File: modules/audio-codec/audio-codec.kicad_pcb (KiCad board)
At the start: 2 copper layers, 1 part, among them U1 TLV320AIC3110IRHBR

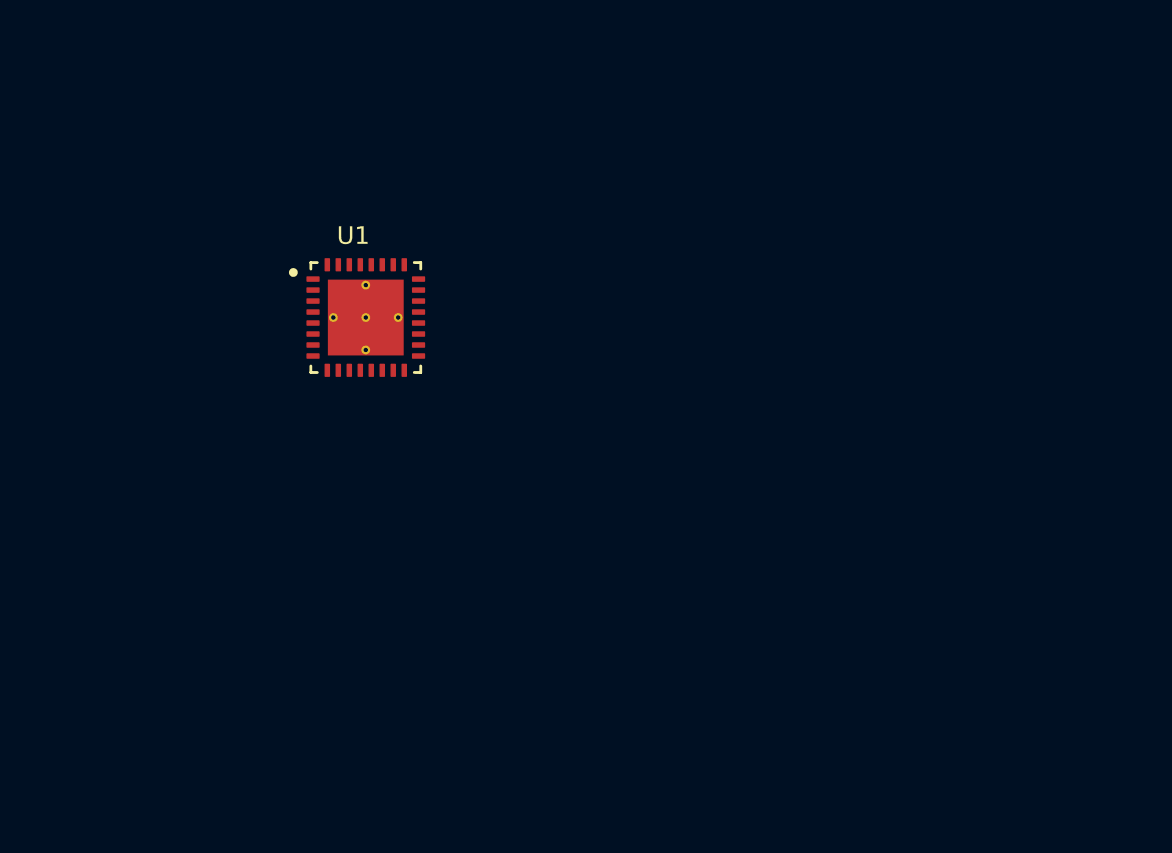
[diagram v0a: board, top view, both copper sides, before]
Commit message: update 2x11 module footprint. Work on PCB layout of audio codec module
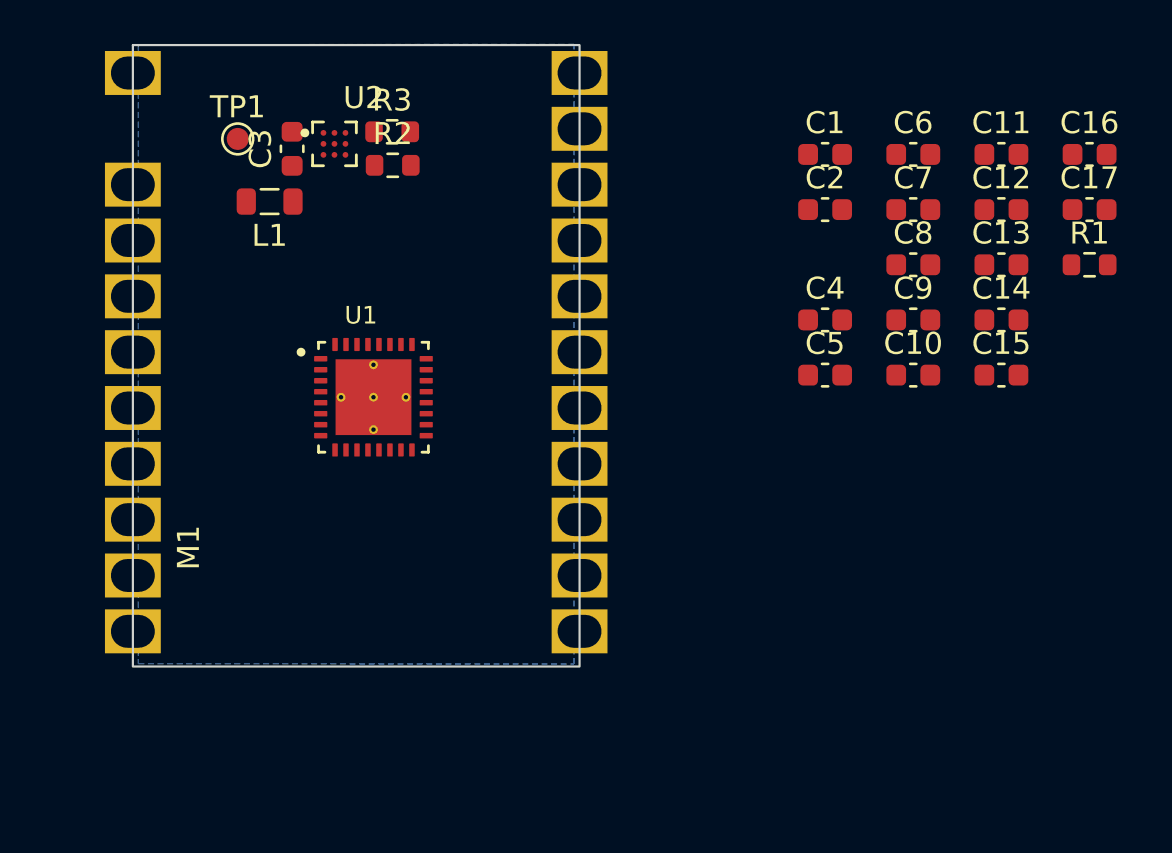
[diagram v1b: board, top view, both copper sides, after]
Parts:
- added C1: 0.1uF, Capacitor_SMD:C_0603_1608Metric, F.Cu at (106.0, 54.1)
- added C10: 0.1uF, Capacitor_SMD:C_0603_1608Metric, F.Cu at (110.0, 64.1)
- added C11: 10uF, Capacitor_SMD:C_0603_1608Metric, F.Cu at (114.0, 54.1)
- added C12: 0.1uF, Capacitor_SMD:C_0603_1608Metric, F.Cu at (114.0, 56.6)
- added C13: 0.1uF, Capacitor_SMD:C_0603_1608Metric, F.Cu at (114.0, 59.1)
- added C14: 10uF, Capacitor_SMD:C_0603_1608Metric, F.Cu at (114.0, 61.6)
- added C15: 10uF, Capacitor_SMD:C_0603_1608Metric, F.Cu at (114.0, 64.1)
- added C16: 47uF, Capacitor_SMD:C_0603_1608Metric, F.Cu at (118.0, 54.1)
- added C17: 47uF, Capacitor_SMD:C_0603_1608Metric, F.Cu at (118.0, 56.6)
- added C2: 10uF, Capacitor_SMD:C_0603_1608Metric, F.Cu at (106.0, 56.6)
- added C3: 10uF, Capacitor_SMD:C_0603_1608Metric, F.Cu at (81.8, 53.8)
- added C4: 0.1uF, Capacitor_SMD:C_0603_1608Metric, F.Cu at (106.0, 61.6)
- added C5: 22uF, Capacitor_SMD:C_0603_1608Metric, F.Cu at (106.0, 64.1)
- added C6: 0.1uF, Capacitor_SMD:C_0603_1608Metric, F.Cu at (110.0, 54.1)
- added C7: 22uF, Capacitor_SMD:C_0603_1608Metric, F.Cu at (110.0, 56.6)
- added C8: 0.1uF, Capacitor_SMD:C_0603_1608Metric, F.Cu at (110.0, 59.1)
- added C9: 10uF, Capacitor_SMD:C_0603_1608Metric, F.Cu at (110.0, 61.6)
- added L1: 2.2uH, Inductor_SMD:L_0805_2012Metric, F.Cu at (80.7, 56.2)
- added M1: ~, MegaCastle:MegaCastle2x11Wide-Module-I13.2x22.25, F.Cu at (84.7, 61.8)
- added R1: 2.2K, Resistor_SMD:R_0603_1608Metric, F.Cu at (118.0, 59.1)
- added R2: 19.6K, Resistor_SMD:R_0603_1608Metric, F.Cu at (86.3, 54.5)
- added R3: 100K, Resistor_SMD:R_0603_1608Metric, F.Cu at (86.3, 53.0)
- added TP1: 1.8V, TestPoint:TestPoint_Pad_D1.0mm, F.Cu at (79.3, 53.4)
- added U2: ADP5301ACBZ-1-R7, audio-codec:BGA9C50P3X3_187X165X66N, F.Cu at (83.7, 53.6)
- moved U1 3.64 mm to (85.5, 65.1)
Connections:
- U1 pad 1: unconnected-(U1-IOVSS-Pad1) -> GND
- U1 pad 10: unconnected-(U1-SCL-Pad10) -> SCL
- U1 pad 11: unconnected-(U1-VOL/MICDET-Pad11) -> Net-(U1-MIC1RP)
- U1 pad 12: unconnected-(U1-MICBIAS-Pad12) -> Net-(U1-MICBIAS)
- U1 pad 14: unconnected-(U1-MIC1RP-Pad14) -> Net-(U1-MIC1RP)
- U1 pad 16: unconnected-(U1-AVSS-Pad16) -> GND
- U1 pad 17: unconnected-(U1-AVDD-Pad17) -> DECOUPLE1
- U1 pad 18: unconnected-(U1-DVSS-Pad18) -> GND
- U1 pad 19: unconnected-(U1-SPLM-Pad19) -> SPEAKER_L_M
- U1 pad 2: unconnected-(U1-IOVDD-Pad2) -> DECOUPLE4
- U1 pad 20: unconnected-(U1-SPLVSS-Pad20) -> GND
- U1 pad 21: unconnected-(U1-SPLVDD-Pad21) -> DECOUPLE1
- U1 pad 22: unconnected-(U1-SPLP-Pad22) -> SPEAKER_L_P
- U1 pad 23: unconnected-(U1-SPRM-Pad23) -> SPEAKER_R_M
- U1 pad 24: unconnected-(U1-SPRVDD-Pad24) -> DECOUPLE1
- U1 pad 25: unconnected-(U1-SPRVSS-Pad25) -> GND
- U1 pad 26: unconnected-(U1-SPRP-Pad26) -> SPEAKER_R_P
- U1 pad 27: unconnected-(U1-HPL-Pad27) -> Net-(U1-HPL)
- U1 pad 28: unconnected-(U1-HPVDD-Pad28) -> DECOUPLE4
- U1 pad 29: unconnected-(U1-HPVSS-Pad29) -> GND
- U1 pad 3: unconnected-(U1-DVDD-Pad3) -> DECOUPLE5
- U1 pad 30: unconnected-(U1-HPR-Pad30) -> Net-(U1-HPR)
- U1 pad 31: unconnected-(U1-~{RESET}-Pad31) -> /RESET
- U1 pad 32: unconnected-(U1-GPIO1-Pad32) -> GPIO1
- U1 pad 33: unconnected-(U1-EP-Pad33) -> GND
- U1 pad 4: unconnected-(U1-DOUT-Pad4) -> I2S_DOUT
- U1 pad 5: unconnected-(U1-DIN-Pad5) -> I2S_DIN
- U1 pad 6: unconnected-(U1-WCLK-Pad6) -> WCLK
- U1 pad 7: unconnected-(U1-BCLK-Pad7) -> I2S_BCLK
- U1 pad 8: unconnected-(U1-MCLK-Pad8) -> I2S_MCLK
- U1 pad 9: unconnected-(U1-SDA-Pad9) -> SDA
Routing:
- added copper zone on B.Cu, net GND
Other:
- board outline added: 20.3 x 28.3 mm

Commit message: more work on audio codec PCB layout
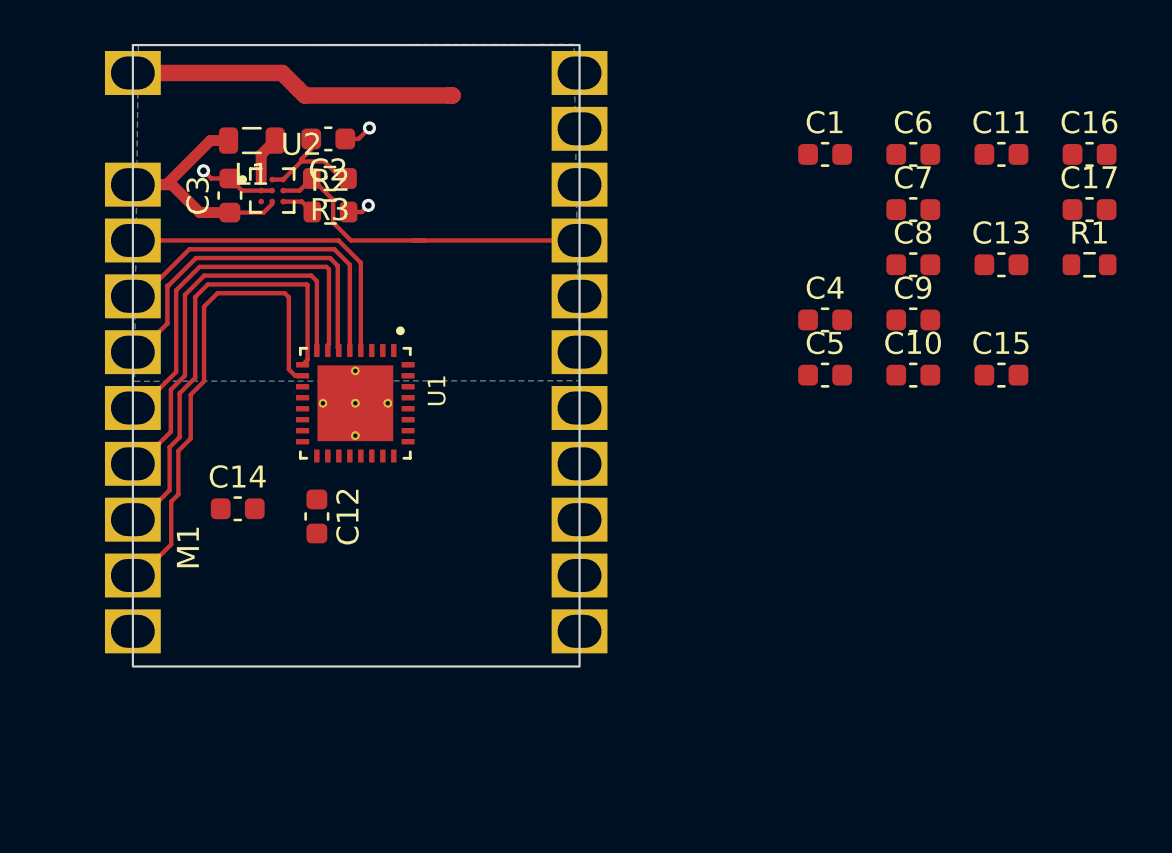
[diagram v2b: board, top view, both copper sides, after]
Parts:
- removed TP1: 1.8V, TestPoint:TestPoint_Pad_D1.0mm
- moved C14 35.8 mm to (79.3, 70.2)
- moved C12 34.1 mm to (82.9, 70.5), turned to -90 degrees
- moved C2 22.8 mm to (83.4, 53.4), turned to 180 degrees
- moved C3 3.54 mm to (78.9, 55.9)
- moved R2 3.54 mm to (83.5, 56.7)
- moved R3 3.54 mm to (83.5, 55.1), turned to 180 degrees
- moved U2 3.54 mm to (80.8, 55.7)
- moved L1 2.89 mm to (79.9, 53.4)
- moved U1 0.87 mm to (84.6, 65.4), turned to -90 degrees
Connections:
- M1 pad 10: unconnected-(M1-Pad10) -> SCL
- M1 pad 15: unconnected-(M1-Pad15) -> V1.8_MODE
- M1 pad 3: unconnected-(M1-Pad3) -> DECOUPLE5
- M1 pad 4: unconnected-(M1-Pad4) -> I2S_DOUT
- M1 pad 5: unconnected-(M1-Pad5) -> I2S_DIN
- M1 pad 6: unconnected-(M1-Pad6) -> WCLK
- M1 pad 7: unconnected-(M1-Pad7) -> I2S_BCLK
- M1 pad 8: unconnected-(M1-Pad8) -> I2S_MCLK
- M1 pad 9: unconnected-(M1-Pad9) -> SDA
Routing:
- net SCL: track 0.00 -> 22.0 mm
- net SDA: track 0.00 -> 20.6 mm
- net I2S_MCLK: track 0.00 -> 18.4 mm
- net I2S_BCLK: track 0.00 -> 17.5 mm
- net WCLK: track 0.00 -> 16.1 mm
- net V1.8_MODE: track 0.00 -> 16.0 mm
- net DECOUPLE1: track 0.00 -> 15.1 mm
- net I2S_DIN: track 0.00 -> 14.9 mm
- net I2S_DOUT: track 0.00 -> 14.8 mm
- net DECOUPLE5: track 0.00 -> 12.3 mm
- net GND: track 0.00 -> 5.83 mm, vias 0 -> 3
- net DECOUPLE4: track 0.00 -> 5.32 mm
- net Net-(U2-SW): track 0.00 -> 2.04 mm
- net Net-(U2-VID): track 0.00 -> 1.52 mm

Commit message: finish placing and routing audio codec module
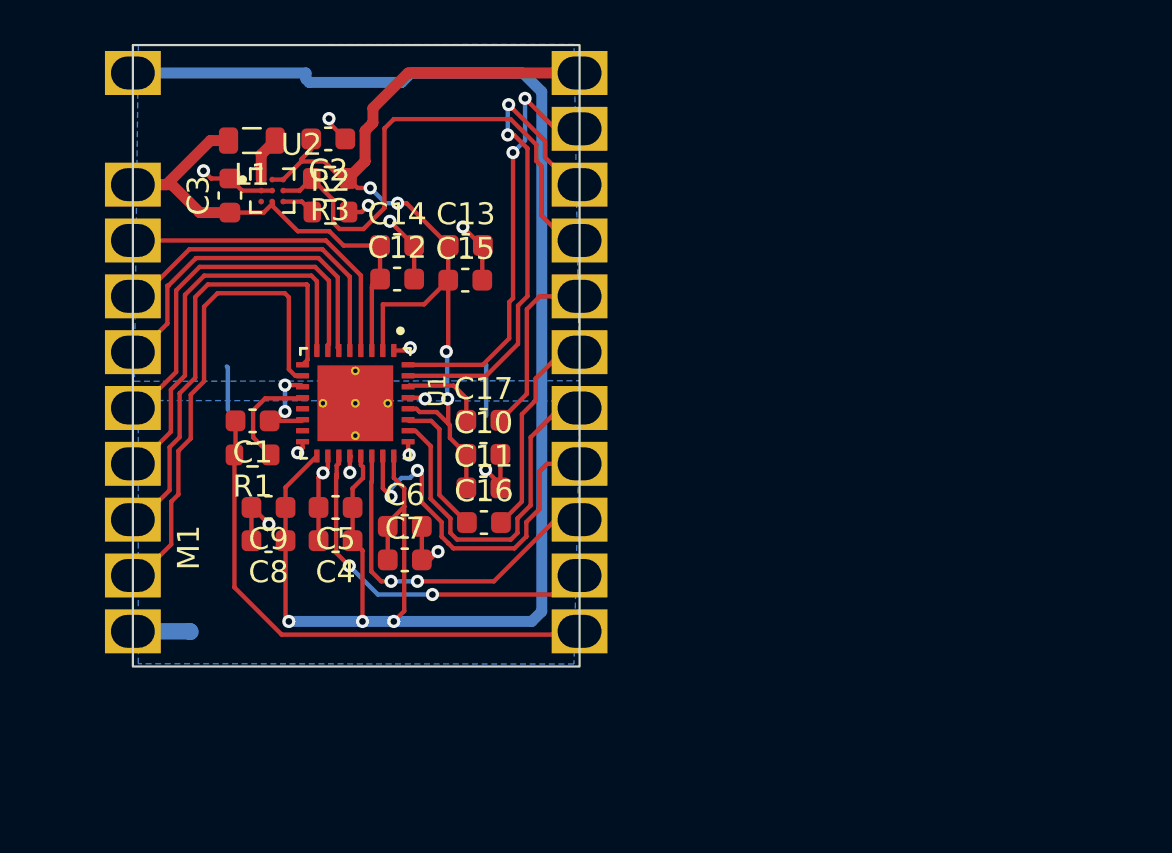
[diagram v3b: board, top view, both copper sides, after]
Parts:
- moved R1 39.0 mm to (80.0, 67.7), turned to 180 degrees
- moved C16 32.2 mm to (90.5, 70.8)
- moved C8 31.9 mm to (80.7, 71.6), turned to 180 degrees
- moved C9 30.5 mm to (80.7, 70.1), turned to 180 degrees
- moved C17 29.2 mm to (90.5, 66.2)
- moved C1 28.7 mm to (80.0, 66.2), turned to 180 degrees
- moved C6 28.7 mm to (86.9, 71.0)
- moved C7 28.1 mm to (86.9, 72.5)
- moved C11 28.0 mm to (90.5, 69.2)
- moved C15 24.8 mm to (89.6, 59.8)
- moved C4 24.4 mm to (83.7, 71.6), turned to 180 degrees
- moved C13 24.4 mm to (89.7, 58.2)
- moved C5 23.1 mm to (83.7, 70.1), turned to 180 degrees
- moved C10 19.9 mm to (90.5, 67.7)
- moved C14 14.0 mm to (86.5, 58.2)
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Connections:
- M1 pad 12: unconnected-(M1-Pad12) -> DECOUPLE4
- M1 pad 13: unconnected-(M1-Pad13) -> GPIO1
- M1 pad 14: unconnected-(M1-Pad14) -> /RESET
- M1 pad 16: unconnected-(M1-Pad16) -> 3.5MM_RIGHT
- M1 pad 17: unconnected-(M1-Pad17) -> 3.5MM_LEFT
- M1 pad 18: unconnected-(M1-Pad18) -> SPEAKER_R_P
- M1 pad 19: unconnected-(M1-Pad19) -> SPEAKER_R_M
- M1 pad 20: unconnected-(M1-Pad20) -> SPEAKER_L_P
- M1 pad 21: unconnected-(M1-Pad21) -> SPEAKER_L_M
- M1 pad 22: unconnected-(M1-Pad22) -> 3.5MM_MIC
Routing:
- net DECOUPLE1: track 15.1 -> 81.6 mm, vias 0 -> 3
- net DECOUPLE4: track 5.32 -> 44.7 mm, vias 0 -> 4
- net GND: track 5.83 -> 34.0 mm, vias 3 -> 14
- net 3.5MM_MIC: track 0.00 -> 24.2 mm
- net /RESET: track 0.00 -> 23.4 mm, vias 0 -> 2
- net GPIO1: track 0.00 -> 19.4 mm, vias 0 -> 2
- net SPEAKER_L_M: track 0.00 -> 16.8 mm, vias 0 -> 2
- net SPEAKER_R_M: track 0.00 -> 16.8 mm, vias 0 -> 2
- net SPEAKER_R_P: track 0.00 -> 16.3 mm
- net SPEAKER_L_P: track 0.00 -> 16.1 mm, vias 0 -> 2
- net DECOUPLE5: track 12.3 -> 23.5 mm
- net 3.5MM_LEFT: track 0.00 -> 9.70 mm
- net 3.5MM_RIGHT: track 0.00 -> 8.19 mm
- net V1.8_MODE: track 16.0 -> 22.9 mm
- net Net-(U1-HPL): track 0.00 -> 6.37 mm
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
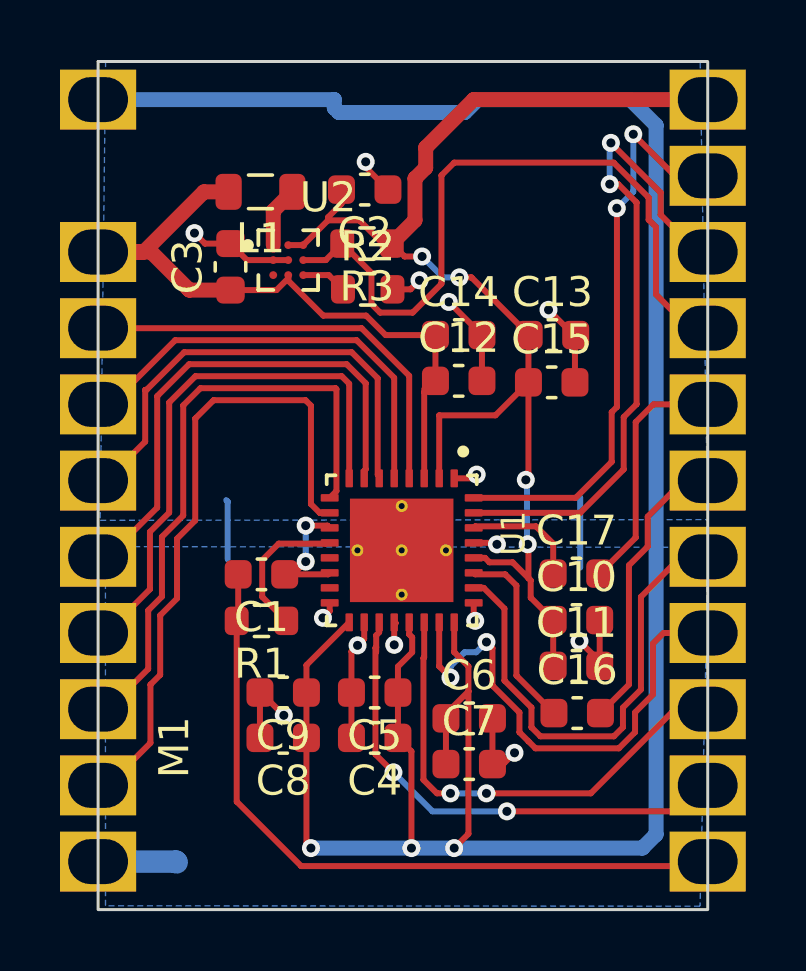
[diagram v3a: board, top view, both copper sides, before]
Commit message: add gnd pads to codec thermal pad, tidy passives and label on rear
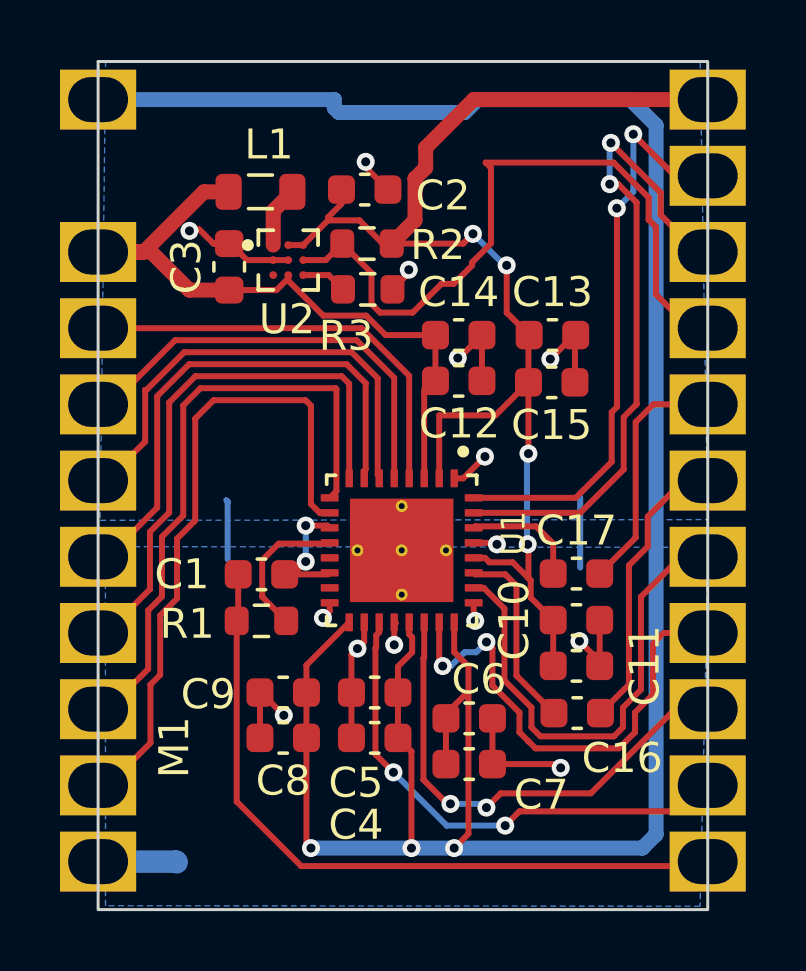
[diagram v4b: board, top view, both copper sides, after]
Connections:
- U1 pad 34: (no net) -> GND
- U1 pad 35: (no net) -> GND
- U1 pad 36: (no net) -> GND
- U1 pad 37: (no net) -> GND
- U1 pad 38: (no net) -> GND
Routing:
- net GND: track 34.0 -> 35.2 mm
- net DECOUPLE4: track 44.7 -> 45.9 mm
- net SPEAKER_R_M: track 16.8 -> 16.2 mm
